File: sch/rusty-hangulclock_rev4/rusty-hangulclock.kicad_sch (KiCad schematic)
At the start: 91 parts, among them J1 Conn_OLED, J2 Conn_OLED, J3 Conn_USB2, J4 USB_C_Receptacle_PowerOnly_6P, Q1 S8050, SW1 RotaryEncoder_Switch_MP, U1 ESP32-C3-WROOM-02, U2 SY8088, U3 DS3231MZ

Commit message: fix: update sch
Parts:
- R2, R6: value 56kΩ -> 5.1kΩ; symbol PCM_JLCPCB-Resistors:0402,56kΩ -> PCM_JLCPCB-Resistors:0402,5.1kΩ; Class Preferred Component -> Basic Component; LCSC C25796 -> C25905; Part 0402WGF5602TCE -> 0402WGF5101TCE; Resistance 56kΩ -> 5.1kΩ; Stock 437393 -> 3534773
- S1: now not fitted; now left out of the parts list
- U1: now fitted; now in the parts list
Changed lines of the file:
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@@
 	)
 	(symbol
-		(lib_id "PCM_JLCPCB-Resistors:0402,56kΩ")
+		(lib_id "PCM_JLCPCB-Resistors:0402,5.1kΩ")
 		(at 383.54 210.82 0)
 		(unit 1)
@@
 			)
 		)
-		(property "Value" "56kΩ"
+		(property "Value" "5.1kΩ"
 			(at 383.54 210.82 90)
 			(do_not_autoplace yes)
@@
 			)
 		)
-		(property "Datasheet" "https://www.lcsc.com/datasheet/lcsc_datasheet_2411221126_UNI-ROYAL-Uniroyal-Elec-0402WGF5602TCE_C25796.pdf"
+		(property "Datasheet" "https://www.lcsc.com/datasheet/lcsc_datasheet_2206010045_UNI-ROYAL-Uniroyal-Elec-0402WGF5101TCE_C25905.pdf"
 			(at 383.54 210.82 0)
 			(effects
@@
 			)
 		)
-		(property "Description" "62.5mW Thick Film Resistors 50V ±100ppm/°C ±1% 56kΩ 0402 Chip Resistor - Surface Mount ROHS"
+		(property "Description" "62.5mW Thick Film Resistors 50V ±100ppm/°C ±1% 5.1kΩ 0402 Chip Resistor - Surface Mount ROHS"
 			(at 383.54 210.82 0)
 			(effects
@@
 			)
 		)
-		(property "LCSC" "C25796"
+		(property "LCSC" "C25905"
 			(at 383.54 210.82 0)
 			(effects
@@
 			)
 		)
-		(property "Stock" "437393"
+		(property "Stock" "3534773"
 			(at 383.54 210.82 0)
 			(effects
@@
 			)
 		)
-		(property "Class" "Preferred Component"
+		(property "Class" "Basic Component"
 			(at 383.54 210.82 0)
 			(effects
@@
 			)
 		)
-		(property "Part" "0402WGF5602TCE"
+		(property "Part" "0402WGF5101TCE"
 			(at 383.54 210.82 0)
 			(effects
@@
 			)
 		)
-		(property "Resistance" "56kΩ"
+		(property "Resistance" "5.1kΩ"
 			(at 383.54 210.82 0)
 			(effects
@@
 		(exclude_from_sim no)
 		(in_bom no)
-		(on_board yes)
+		(on_board no)
 		(dnp yes)
 		(fields_autoplaced yes)
@@
 	)
 	(symbol
-		(lib_id "PCM_JLCPCB-Resistors:0402,56kΩ")
+		(lib_id "PCM_JLCPCB-Resistors:0402,5.1kΩ")
 		(at 391.16 210.82 0)
 		(unit 1)
@@
 			)
 		)
-		(property "Value" "56kΩ"
+		(property "Value" "5.1kΩ"
 			(at 391.16 210.82 90)
 			(do_not_autoplace yes)
@@
 			)
 		)
-		(property "Datasheet" "https://www.lcsc.com/datasheet/lcsc_datasheet_2411221126_UNI-ROYAL-Uniroyal-Elec-0402WGF5602TCE_C25796.pdf"
+		(property "Datasheet" "https://www.lcsc.com/datasheet/lcsc_datasheet_2206010045_UNI-ROYAL-Uniroyal-Elec-0402WGF5101TCE_C25905.pdf"
 			(at 391.16 210.82 0)
 			(effects
@@
 			)
 		)
-		(property "Description" "62.5mW Thick Film Resistors 50V ±100ppm/°C ±1% 56kΩ 0402 Chip Resistor - Surface Mount ROHS"
+		(property "Description" "62.5mW Thick Film Resistors 50V ±100ppm/°C ±1% 5.1kΩ 0402 Chip Resistor - Surface Mount ROHS"
 			(at 391.16 210.82 0)
 			(effects
@@
 			)
 		)
-		(property "LCSC" "C25796"
+		(property "LCSC" "C25905"
 			(at 391.16 210.82 0)
 			(effects
@@
 			)
 		)
-		(property "Stock" "437393"
+		(property "Stock" "3534773"
 			(at 391.16 210.82 0)
 			(effects
@@
 			)
 		)
-		(property "Class" "Preferred Component"
+		(property "Class" "Basic Component"
 			(at 391.16 210.82 0)
 			(effects
@@
 			)
 		)
-		(property "Part" "0402WGF5602TCE"
+		(property "Part" "0402WGF5101TCE"
 			(at 391.16 210.82 0)
 			(effects
@@
 			)
 		)
-		(property "Resistance" "56kΩ"
+		(property "Resistance" "5.1kΩ"
 			(at 391.16 210.82 0)
 			(effects
@@
 		(unit 1)
 		(exclude_from_sim no)
-		(in_bom no)
+		(in_bom yes)
 		(on_board yes)
-		(dnp yes)
+		(dnp no)
 		(fields_autoplaced yes)
 		(property "Reference" "U1"
@@
 		(unit 1)
 		(exclude_from_sim no)
-		(in_bom yes)
+		(in_bom no)
 		(on_board yes)
-		(dnp no)
+		(dnp yes)
 		(fields_autoplaced yes)
 		(property "Reference" "S1"

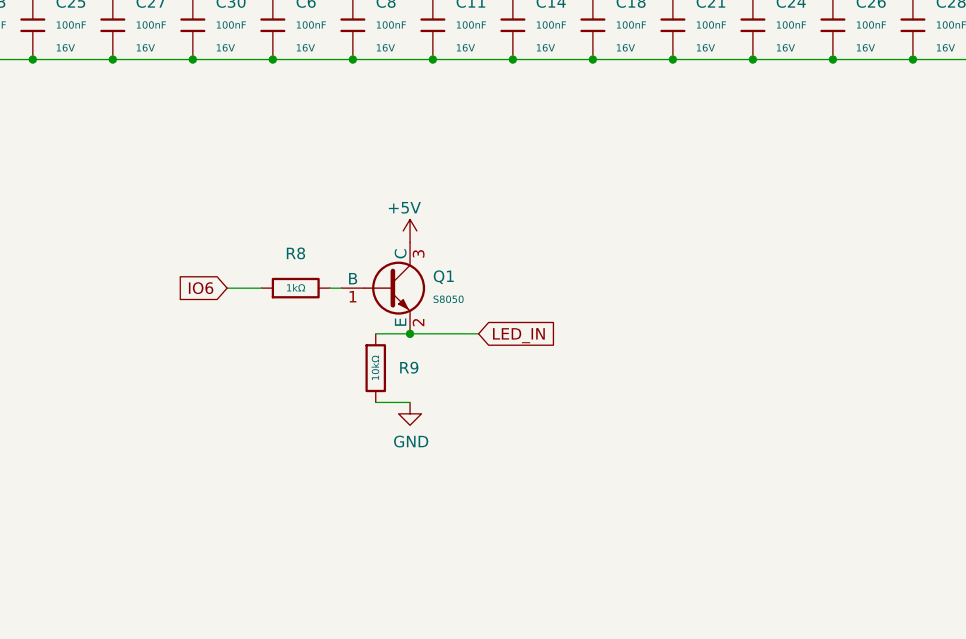
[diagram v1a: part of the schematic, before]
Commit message: refactor: update dependencies and improve task management
- Updated the `futures` dependency in `Cargo.toml` to disable default features and enable specific ones for better control.
- Incremented software version in `flash.sh` and `Makefile_homin` for consistency.
- Enhanced the schematic by adding new junctions and wires, while removing unnecessary elements for clarity.
- Refactored the main application logic in `main.rs` to streamline task execution and improve error handling.
- Commented out unused time synchronization logic in `net.rs` to simplify the codebase.
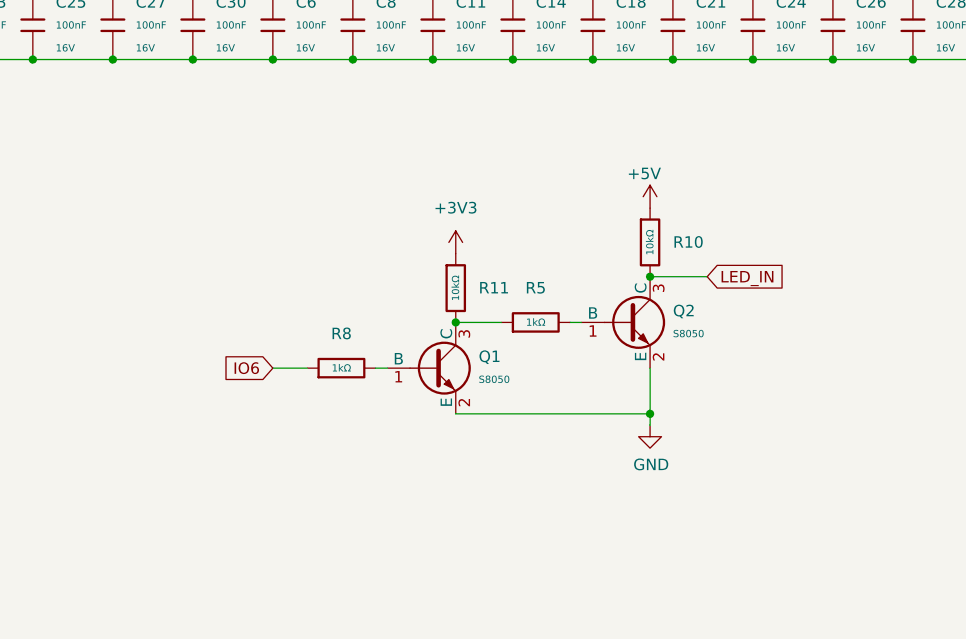
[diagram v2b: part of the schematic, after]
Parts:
- removed R9: 10kΩ, PCM_JLCPCB:R_0402, symbol PCM_JLCPCB-Resistors:0402,10kΩ
- added Q2: S8050, PCM_JLCPCB:Q_SOT-23, symbol PCM_JLCPCB-Transistors:NPN,S8050
- added R10, R11: 10kΩ, PCM_JLCPCB:R_0402, symbol PCM_JLCPCB-Resistors:0402,10kΩ
- added R5: 1kΩ, PCM_JLCPCB:R_0402, symbol PCM_JLCPCB-Resistors:0402,1kΩ
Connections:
- net +3V3: now also R11.1
- net +5V: now also R10.1; no longer Q1.3 (C)
- net GND: now also Q1.2 (E), Q2.2 (E)
- net LED_IN: now also Q2.3 (C), R10.2; no longer Q1.2 (E)
- new net: Q1.3 (C), R11.2, R5.1
- new net: Q2.1 (B), R5.2
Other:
- moved on the sheet: Q1, R8
